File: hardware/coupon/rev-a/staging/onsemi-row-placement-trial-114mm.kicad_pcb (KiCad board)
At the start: 6 copper layers, 114 x 32.5 mm, 483 parts, among them J1 USB4505-03-0-A, J2 S2B-PH-SM4-TB, SW1 EVQP7J01P, SW2 JS202011JCQN, U1 TLC59581RTQT, U11 SN74LVC1G04DBVR, U17 SN74LVC1G11DBVR, U2 74HC4514PW,118, U23 SN74LVC1G06DBVR, U24 SN74LVC2G17DBVR, U25 SN74LVC2G17DBVR, U29 TPS70933DBVR, U3 ESP32-S3-WROOM-1U-N16R8, U31 TUSB320LAIRWBR, U32 TS3USB31ERSER, U33 TPD4E05U06DQAR, U34 TPS3808G01DBVR, U35 MAX17048G+T10, U36 TPS631000DRLR, U37 TPS63020DSJT, U38 2.5V shunt, U39 TMP390A2DRLR, U40 SN74AUP1G125DBVR, U41 BQ24074RGTR, U42 SN74AUP1G125DBVR, U43 SN74AUP1G125DBVR, U44 TPS259474ARPWR, U45 TPS259474ARPWR, U46 TCA9517ADGKR, U47 TPS3823A-33DBVR, U48 SN74LVC1G04DSFR, U49 SN74LVC1G74RSER, U50 SN74LVC1G74RSER, U51 SN74LVC1G11DRYR, U52 SN74LVC1G08DSFR, U53 TLV6700DSER, U54 SN74LVC2G00DCUR, U55 SN74LVC2G08DCUR

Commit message: Connect USB shell returns in 114 mm routing trial
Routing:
- net GND: track 170.2 -> 182.1 mm

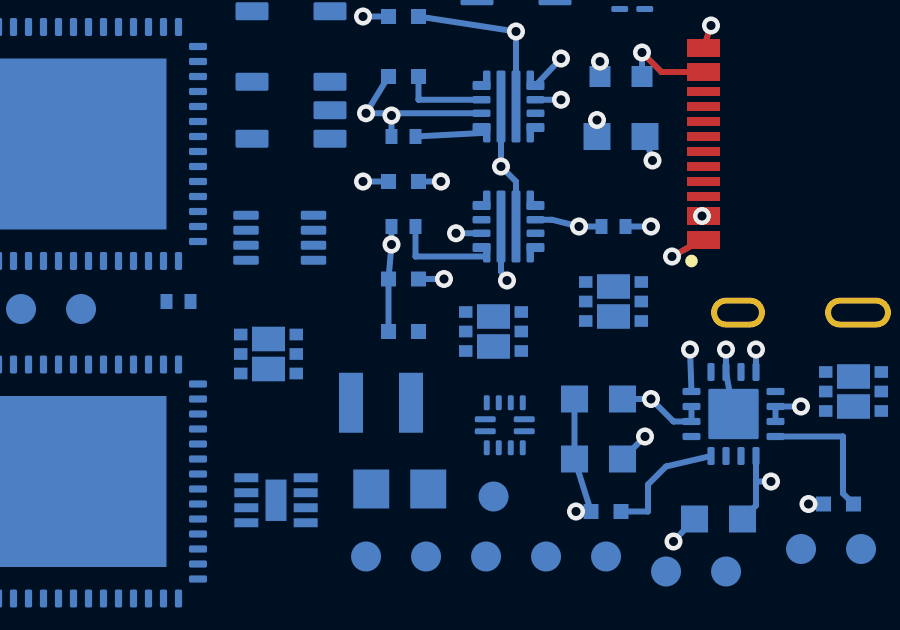
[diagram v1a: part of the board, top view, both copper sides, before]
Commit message: Route E1 current-limit network on 114 mm trial
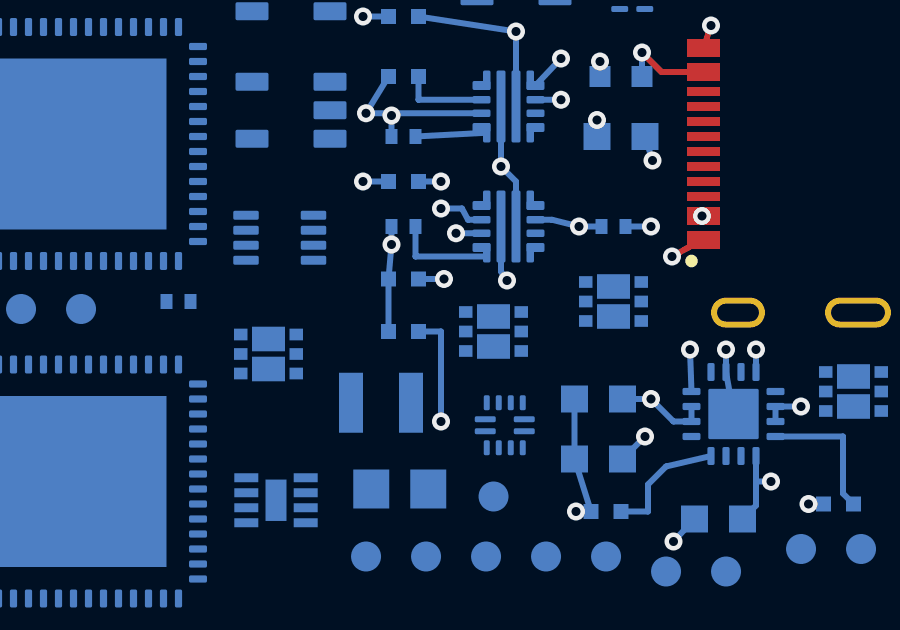
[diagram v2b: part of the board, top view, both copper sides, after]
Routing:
- net E1_ILM: track 0.00 -> 13.5 mm, vias 0 -> 2

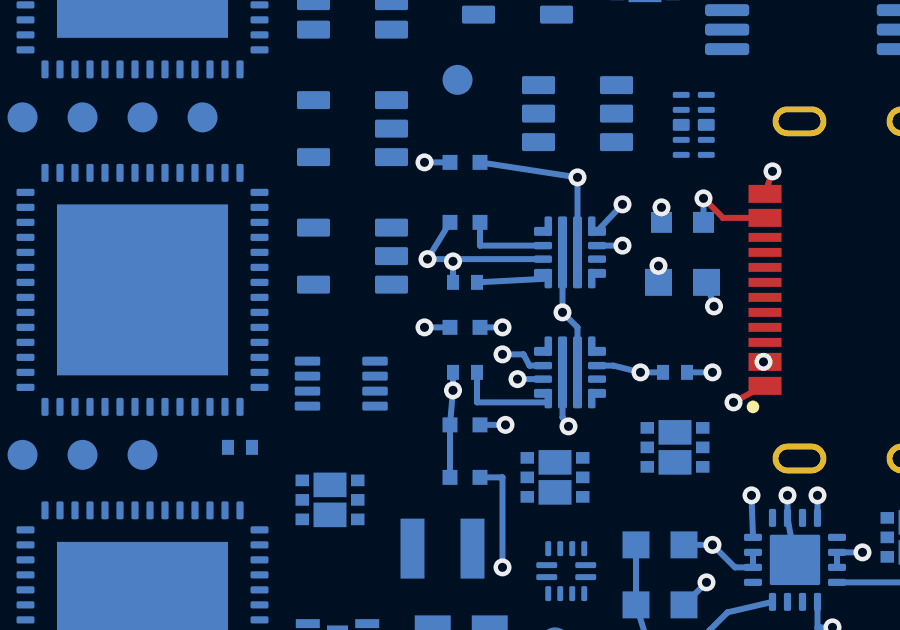
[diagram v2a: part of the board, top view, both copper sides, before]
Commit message: Route local charger permission to E1 enable
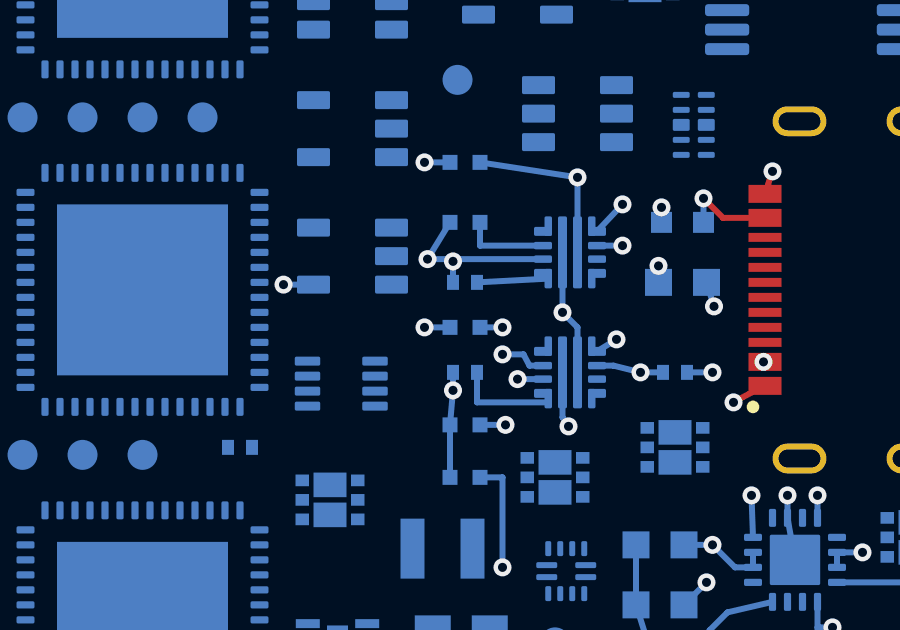
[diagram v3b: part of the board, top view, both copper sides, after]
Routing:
- net CHARGER_GATE_EN: track 0.00 -> 16.1 mm, vias 0 -> 2

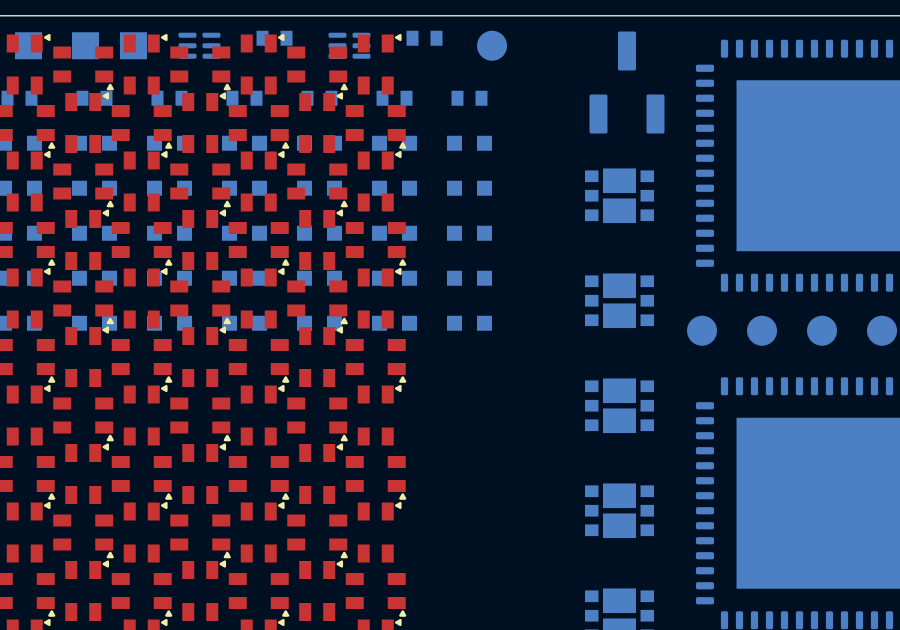
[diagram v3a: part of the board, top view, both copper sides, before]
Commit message: Connect E1 enable bias resistors on 114 mm trial
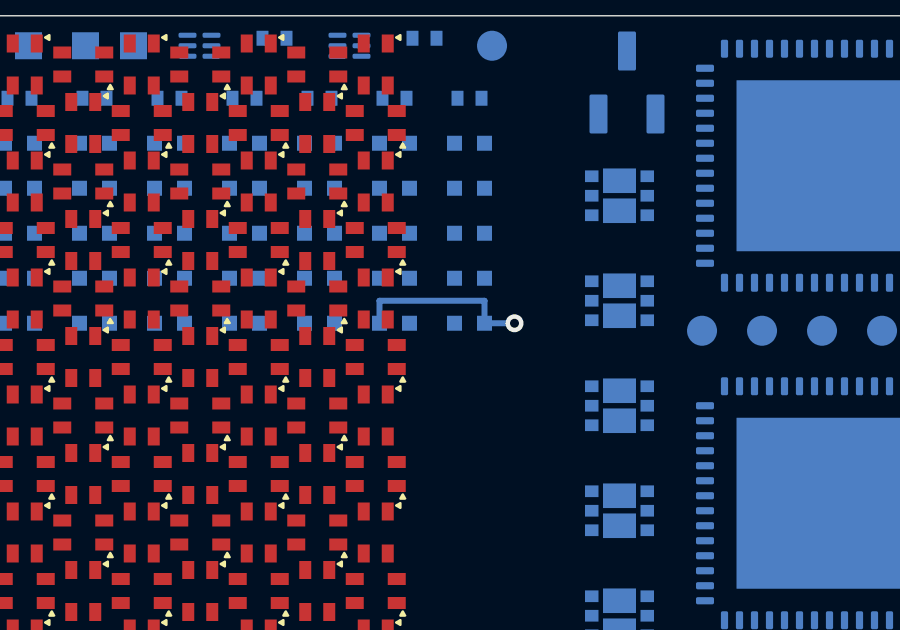
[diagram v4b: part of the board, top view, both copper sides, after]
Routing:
- net CHARGER_GATE_EN: track 16.1 -> 38.2 mm, vias 2 -> 3

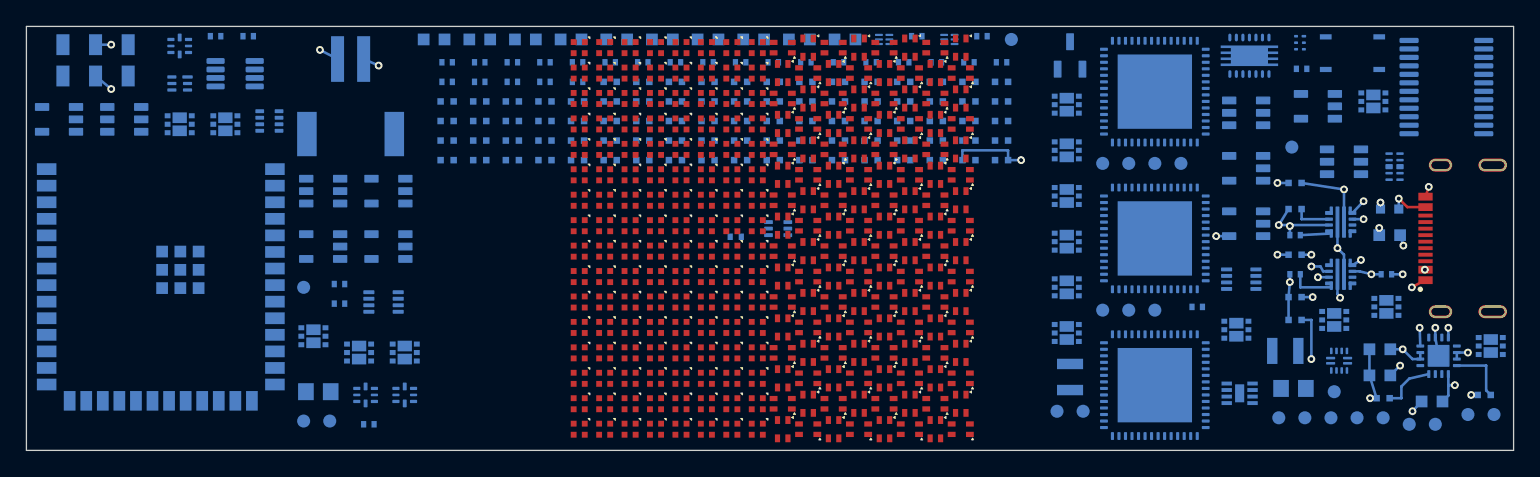
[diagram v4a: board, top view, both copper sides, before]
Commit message: Route charger inhibit node and local supervisor links on 114mm trial
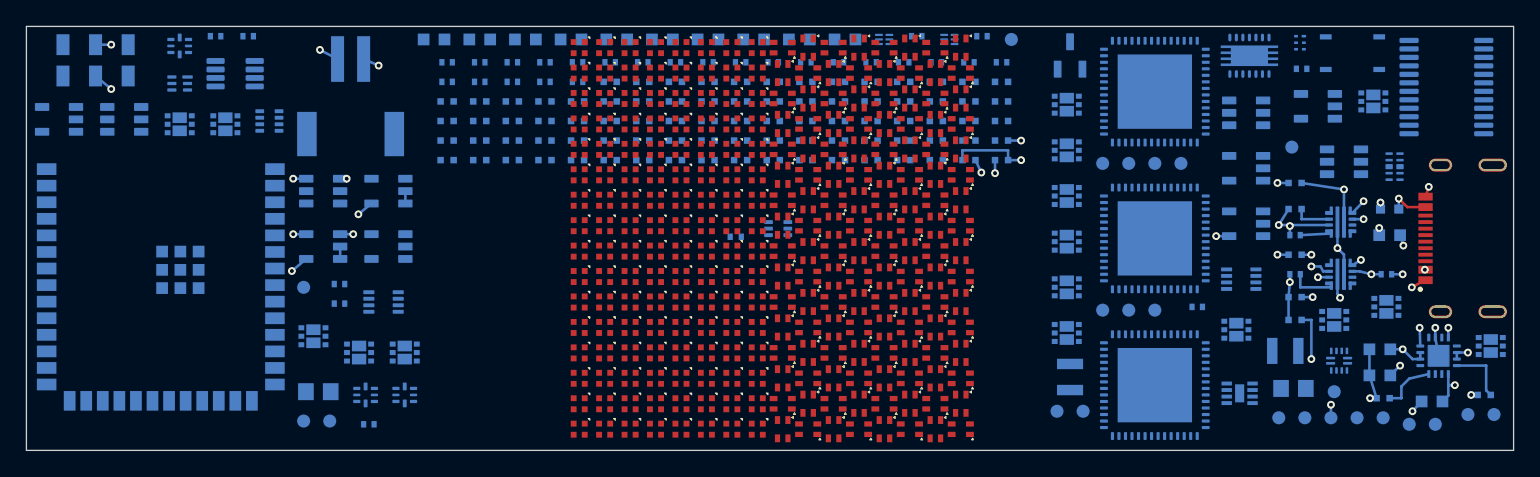
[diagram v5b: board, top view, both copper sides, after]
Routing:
- net CHARGER_GATE_EN: track 38.2 -> 126.6 mm, vias 3 -> 6
- net +3V3_USB: track 0.00 -> 12.2 mm, vias 0 -> 4
- net GND: track 182.1 -> 191.8 mm, vias 16 -> 17
- net USB_RAW_LOGIC_READY: track 0.00 -> 5.96 mm, vias 0 -> 2

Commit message: Route source charge request and local logic returns
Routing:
- net GND: track 191.8 -> 206.9 mm, vias 17 -> 18
- net +3V3_USB: track 12.2 -> 24.2 mm, vias 4 -> 6
- net USB_CHARGE_REQ: track 0.00 -> 9.69 mm, vias 0 -> 2

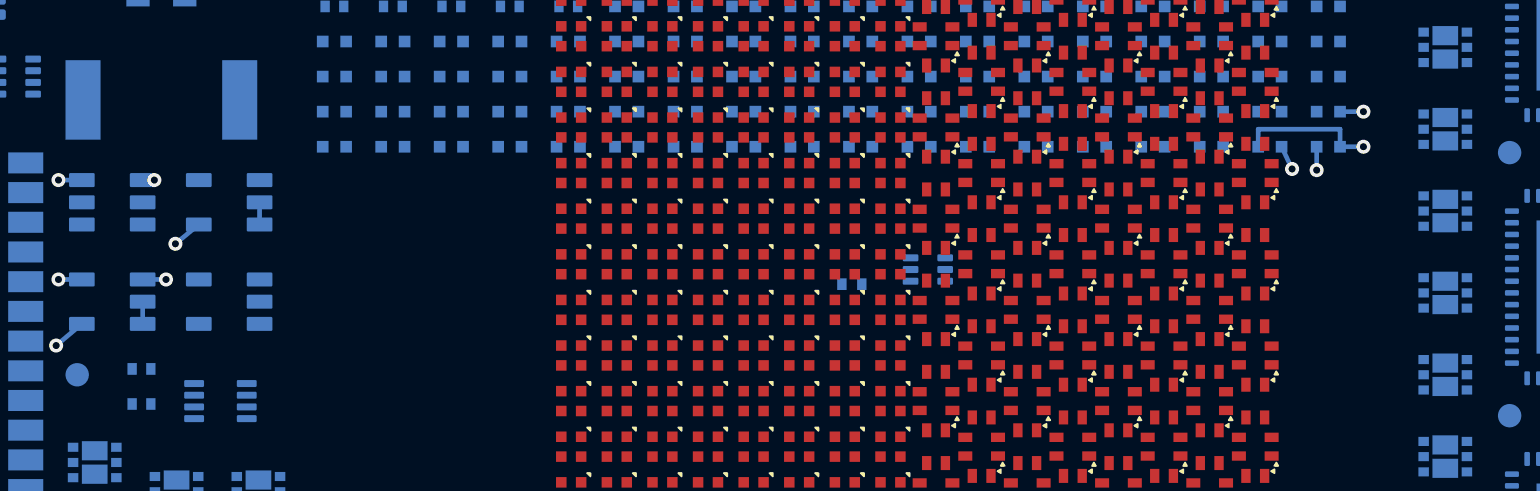
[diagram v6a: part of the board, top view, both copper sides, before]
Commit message: Route temperature inhibit and remaining sink grounds
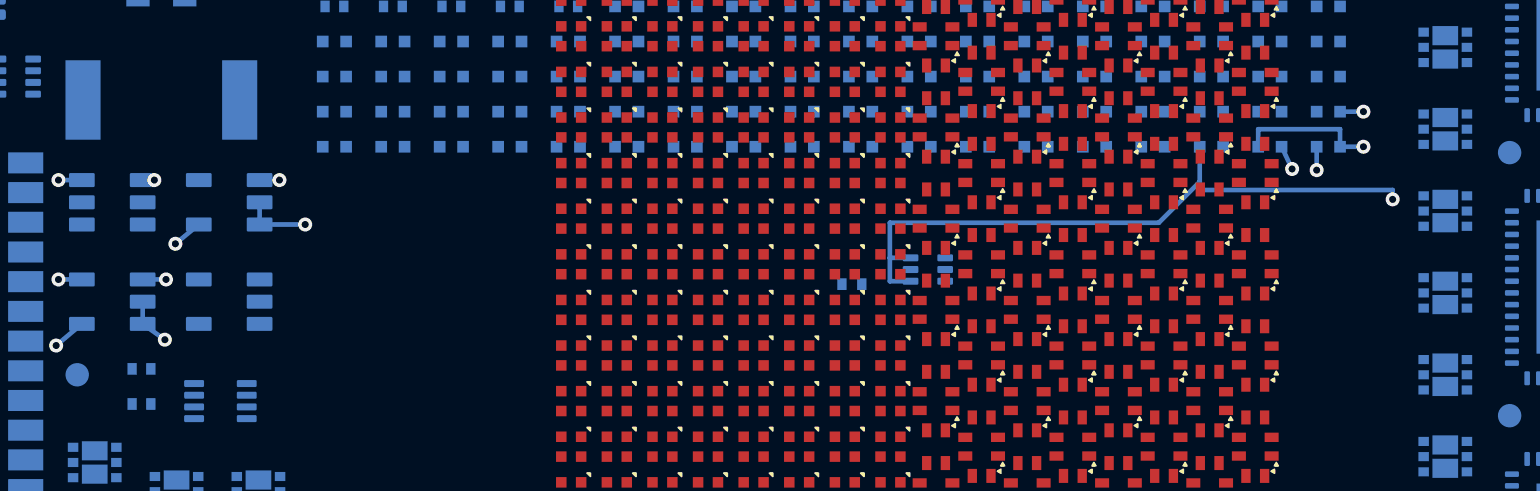
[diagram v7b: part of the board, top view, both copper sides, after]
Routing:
- net TEMP_OK: track 0.00 -> 82.3 mm, vias 0 -> 2
- net GND: track 206.9 -> 229.2 mm, vias 18 -> 20

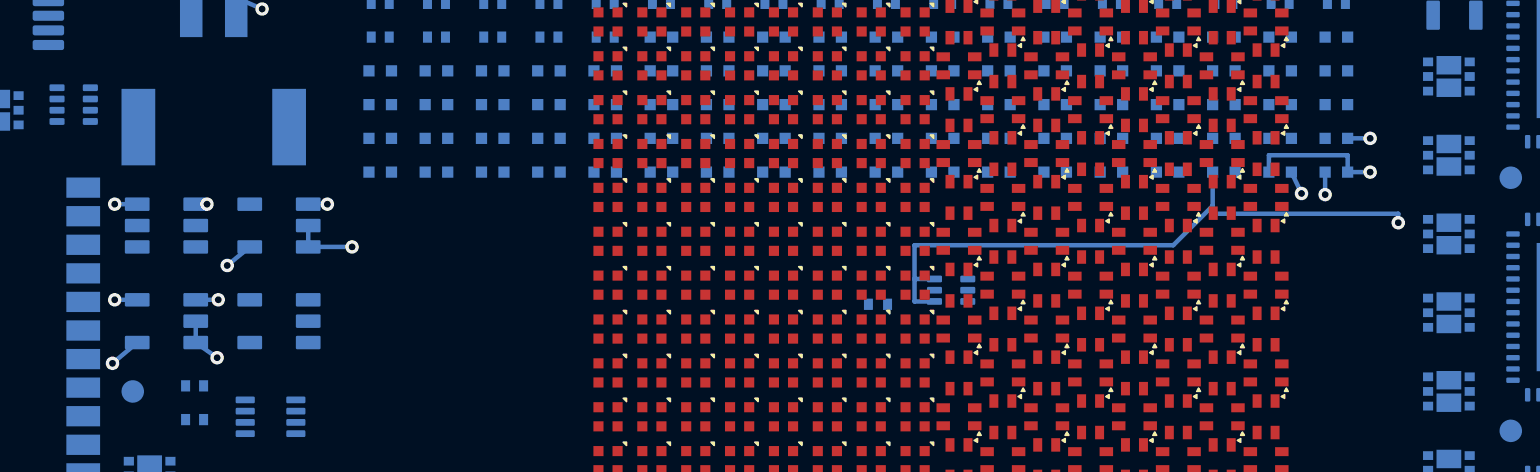
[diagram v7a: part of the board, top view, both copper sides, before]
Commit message: Join charger permission logic supply and temperature sensor returns
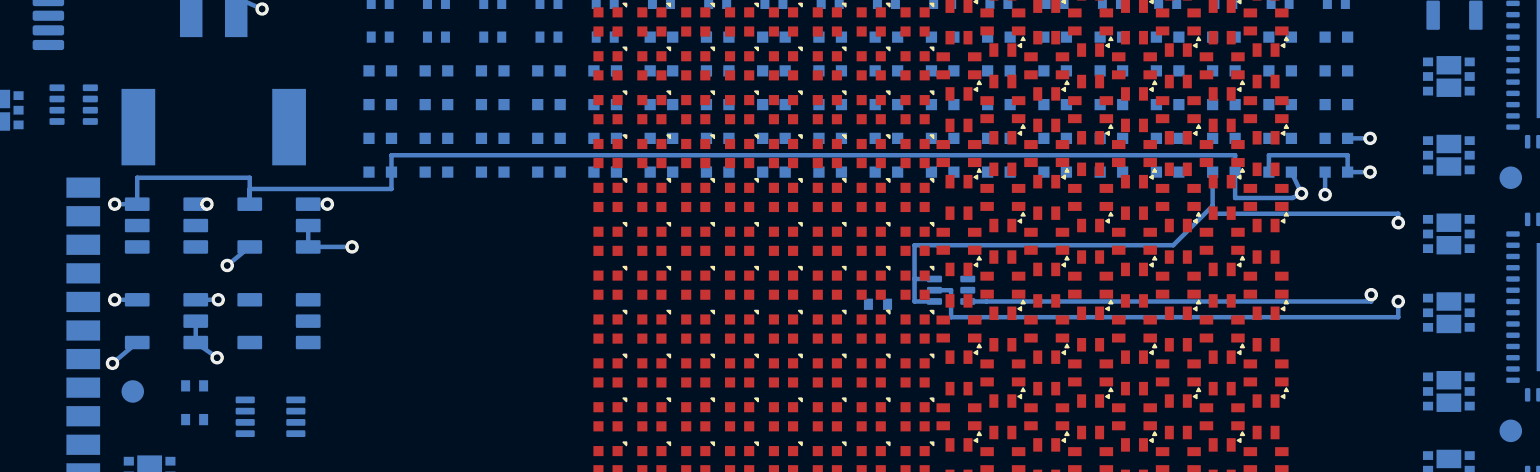
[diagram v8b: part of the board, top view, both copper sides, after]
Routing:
- net +3V3_USB: track 24.2 -> 130.5 mm, vias 6 -> 7
- net GND: track 229.2 -> 250.4 mm, vias 20 -> 21
